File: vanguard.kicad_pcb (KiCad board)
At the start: 4 copper layers, 22 x 33.4 mm, 26 parts, among them J1 Conn_01x02, J2 USB_C_Receptacle, SW1 Switch_Tactile_CnK, U1 ATtiny3227-M, U2 MCP73831-2-OT, U5 AP63203WU

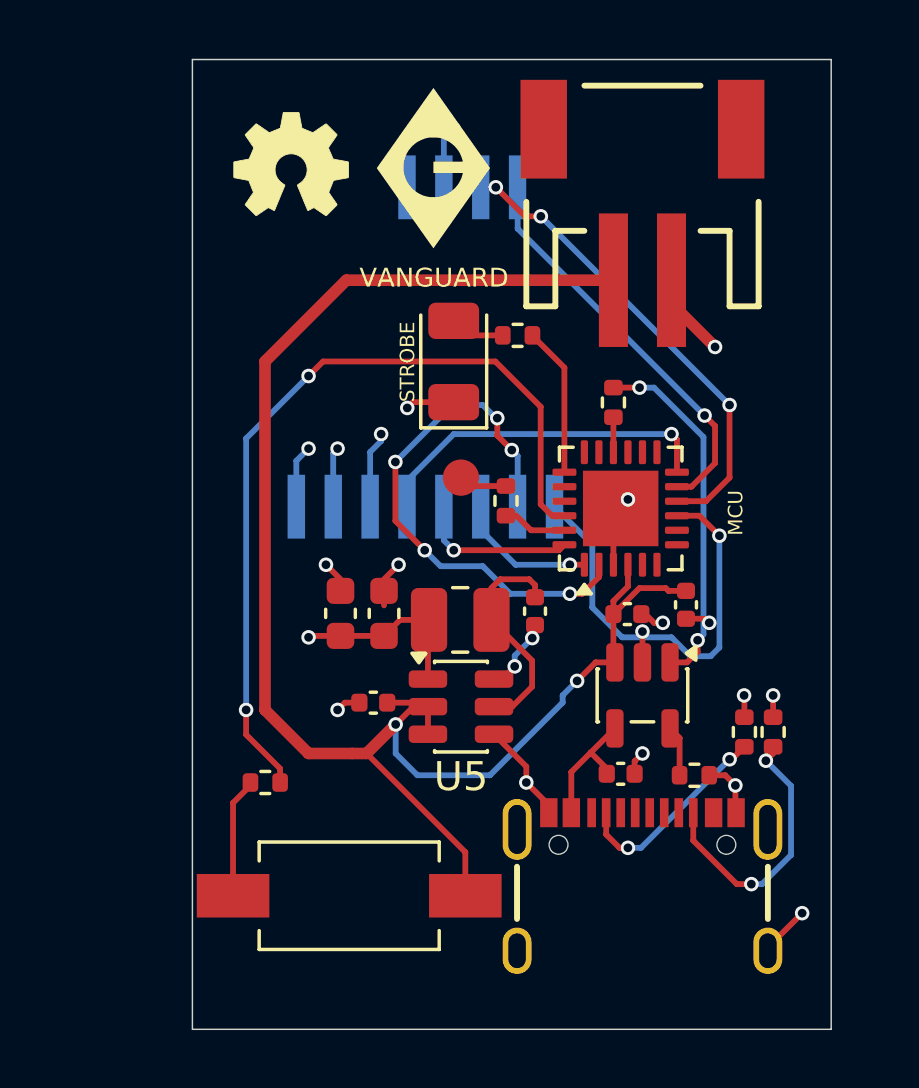
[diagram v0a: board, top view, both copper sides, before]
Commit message: basic code plus added UART
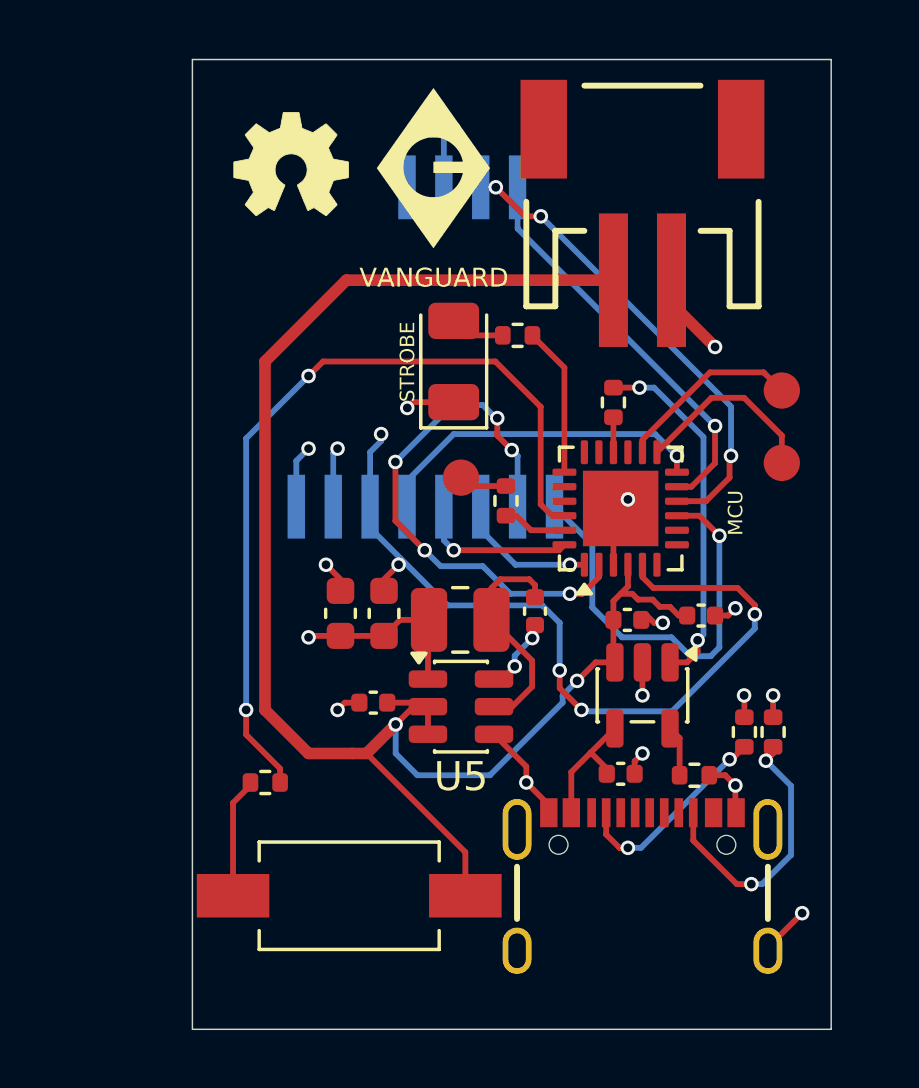
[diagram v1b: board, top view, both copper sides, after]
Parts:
- added TP2: 1.25mm, PCM_SparkFun-Connector:TestPoint-1.25mm, F.Cu at (147.3, 58.0)
- added TP3: 1.25mm, PCM_SparkFun-Connector:TestPoint-1.25mm, F.Cu at (147.3, 60.5)
- moved C2 0.64 mm to (144.5, 65.8), turned to 180 degrees
- moved C1 0.20 mm to (142.0, 65.9)
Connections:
- A1 pad 6: GND -> /SS
- U1 pad 13: unconnected-(U1-PB3-Pad13) -> /RX
- U1 pad 14: unconnected-(U1-PB2-Pad14) -> /TX
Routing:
- net /SS: track 0.00 -> 24.2 mm, vias 0 -> 3
- net /RX: track 0.00 -> 6.56 mm
- net /TX: track 0.00 -> 6.45 mm
- net GND: track 108.9 -> 113.1 mm
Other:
- board text added: "TX RX"

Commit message: done + optimizations
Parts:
- removed TP2, TP3: 1.25mm, PCM_SparkFun-Connector:TestPoint-1.25mm
- added J3: Conn_01x04_Pin, PCM_SparkFun-Connector:JST_1x04_P1.0mm_Horizontal_SMD, F.Cu at (127.1, 57.3)
- added J4: Conn_01x02, Connector_PinHeader_1.27mm:PinHeader_1x02_P1.27mm_Vertical, F.Cu at (148.2, 57.8)
- added REF**: MountingHole_2.2mm_M2_DIN965_Pad, MountingHole:MountingHole_2.2mm_M2_DIN965_Pad, F.Cu at (125.2, 49.2)
- added REF**: MountingHole_2.2mm_M2_DIN965_Pad, MountingHole:MountingHole_2.2mm_M2_DIN965_Pad, F.Cu at (125.2, 77.2)
- moved SW1 0.90 mm to (132.4, 74.5)
- moved J1 0.75 mm to (142.5, 49.8)
- moved R1 0.50 mm to (142.0, 58.4)
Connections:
- R1 pad 2: Net-(U1-PB0) -> Net-(U1-PB1)
- R6 pad 2: Net-(U1-PC2) -> Net-(U1-PC1)
- U1 pad 15: unconnected-(U1-PB1-Pad15) -> Net-(U1-PB1)
- U1 pad 16: Net-(U1-PB0) -> /SDA
- U1 pad 18: unconnected-(U1-PC1-Pad18) -> Net-(U1-PC1)
- U1 pad 19: Net-(U1-PC2) -> /SCL
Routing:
- net /SDA: track 0.00 -> 17.2 mm, vias 0 -> 2
- net /SCL: track 0.00 -> 16.5 mm, vias 0 -> 2
- net Net-(U1-PC2): track 5.17 -> 0.00 mm
- net 3.3V: track 15.1 -> 20.0 mm, vias 2 -> 3
- net Net-(U1-PC1): track 0.00 -> 4.78 mm
- net GND: track 113.1 -> 117.3 mm
- net Net-(U1-PB1): track 0.00 -> 1.20 mm
- net Net-(U1-PB0): track 1.20 -> 0.00 mm
- net Net-(R7-Pad2): track 4.15 -> 3.25 mm
- net /TX: track 6.45 -> 7.29 mm
- net VBATT: track 58.0 -> 57.5 mm
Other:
- board size 22 x 33.4 mm -> 27.5 x 33.4 mm
- board text added: "I2C"
- board text added: "UPDI"

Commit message: clean routing
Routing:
- net /RW_SW: track 14.8 -> 17.5 mm
- net /RX: track 6.35 -> 6.95 mm
- net /BUSY: track 16.4 -> 16.9 mm
- net VBATT: track 57.5 -> 58.0 mm

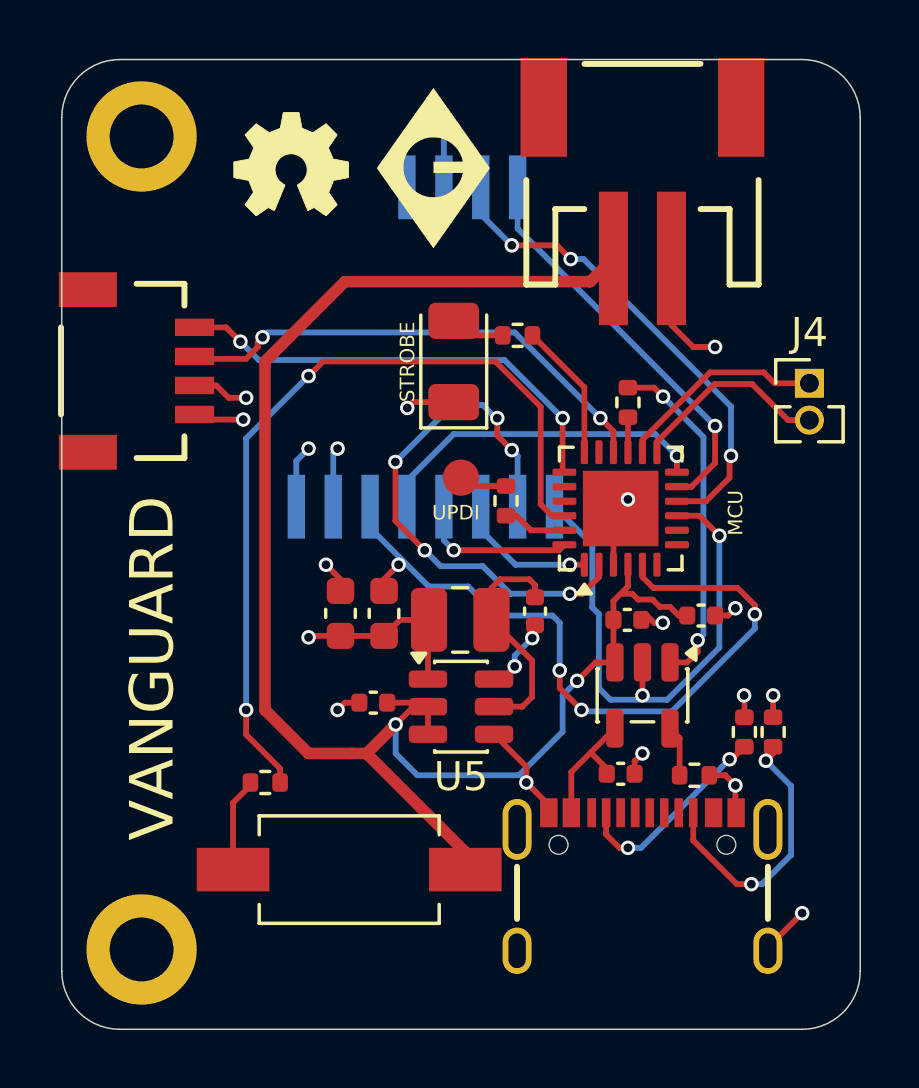
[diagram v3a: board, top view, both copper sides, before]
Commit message: cleaned up routing, fixed mistakes, implemented ETD initialization
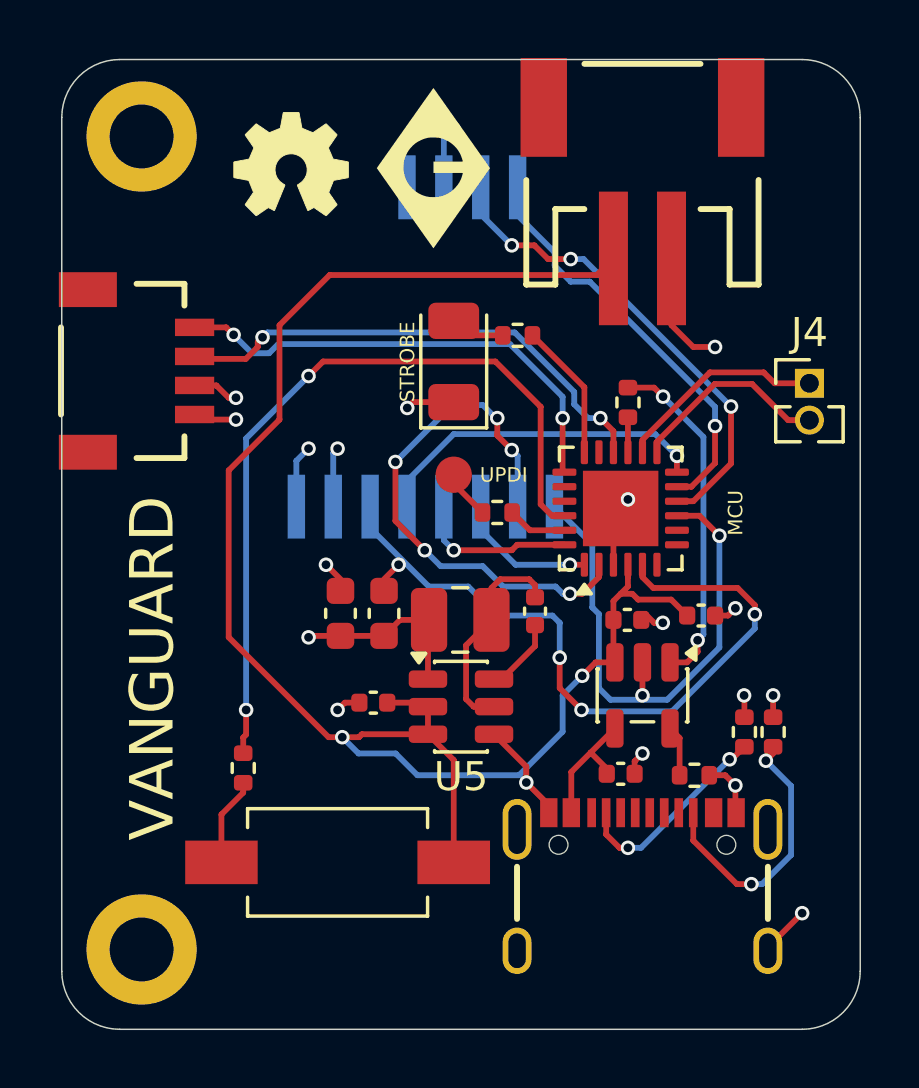
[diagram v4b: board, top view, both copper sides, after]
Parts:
- moved R7 0.91 mm to (128.8, 71.0), turned to -90 degrees
- moved R2 0.50 mm to (137.5, 62.2), turned to 180 degrees
- moved SW1 0.47 mm to (132.0, 74.2)
- moved TP1 0.27 mm to (136.0, 60.9)
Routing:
- net Net-(U1-PC5): track 28.6 -> 27.1 mm
- net VBATT: track 58.0 -> 59.4 mm
- net /SCL: track 16.5 -> 17.3 mm
- net Net-(U5-SW): track 7.91 -> 7.39 mm
- net Net-(U5-BST): track 2.60 -> 2.74 mm, vias 2 -> 0

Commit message: hw check 3
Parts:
- moved R3 2.33 mm to (144.9, 69.0), turned to -90 degrees
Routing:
- net GND: track 117.3 -> 119.9 mm, vias 18 -> 17
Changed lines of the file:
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@@
 	(footprint "PCM_SparkFun-Resistor:R_0402_1005Metric"
 		(layer "F.Cu")
-		(at 144.29 71.25 180)
+		(at 144.9 69 -90)
 		(descr "Resistor SMD 0402 (1005 Metric), square (rectangular) end terminal, IPC_7351 nominal, (Body size source: IPC-SM-782 page 72, https://www.pcb-3d.com/wordpress/wp-content/uploads/ipc-sm-782a_amendment_1_and_2.pdf), generated with kicad-footprint-generator")
 		(tags "SparkFun resistor")
 		(property "Reference" "R3"
-			(at 0 -1.17 0)
+			(at 0 -1.17 90)
 			(layer "F.Fab")
 			(effects
@@
 		)
 		(property "Value" "2.2k"
-			(at 0 1.17 0)
+			(at 0 1.17 90)
 			(layer "F.Fab")
 			(effects
@@
 		)
 		(property "Datasheet" "https://www.vishay.com/docs/20035/dcrcwe3.pdf"
-			(at 0 0 180)
+			(at 0 0 270)
 			(unlocked yes)
 			(layer "F.Fab")
@@
 		)
 		(property "Description" "Resistor"
-			(at 0 0 180)
+			(at 0 0 270)
 			(unlocked yes)
 			(layer "F.Fab")
@@
 		)
 		(property "PROD_ID" "RES-25566"
-			(at 0 0 180)
+			(at 0 0 270)
 			(unlocked yes)
 			(layer "F.Fab")
@@
 		)
 		(fp_line
-			(start 0.93 0.47)
-			(end -0.93 0.47)
+			(start -0.93 0.47)
+			(end -0.93 -0.47)
 			(stroke
 				(width 0.05)
@@
 		)
 		(fp_line
-			(start 0.93 -0.47)
-			(end 0.93 0.47)
+			(start 0.93 0.47)
+			(end -0.93 0.47)
 			(stroke
 				(width 0.05)
@@
 		)
 		(fp_line
-			(start -0.93 0.47)
-			(end -0.93 -0.47)
+			(start -0.93 -0.47)
+			(end 0.93 -0.47)
 			(stroke
 				(width 0.05)
@@
 		)
 		(fp_line
-			(start -0.93 -0.47)
-			(end 0.93 -0.47)
+			(start 0.93 -0.47)
+			(end 0.93 0.47)
 			(stroke
 				(width 0.05)
@@
 		)
 		(fp_line
-			(start 0.525 0.27)
-			(end -0.525 0.27)
+			(start -0.525 0.27)
+			(end -0.525 -0.27)
 			(stroke
 				(width 0.1)
@@
 		)
 		(fp_line
-			(start 0.525 -0.27)
-			(end 0.525 0.27)
+			(start 0.525 0.27)
+			(end -0.525 0.27)
 			(stroke
 				(width 0.1)
@@
 		)
 		(fp_line
-			(start -0.525 0.27)
-			(end -0.525 -0.27)
+			(start -0.525 -0.27)
+			(end 0.525 -0.27)
 			(stroke
 				(width 0.1)
@@
 		)
 		(fp_line
-			(start -0.525 -0.27)
-			(end 0.525 -0.27)
+			(start 0.525 -0.27)
+			(end 0.525 0.27)
 			(stroke
 				(width 0.1)
@@
 		)
 		(pad "1" smd roundrect
-			(at -0.51 0 180)
+			(at -0.51 0 270)
 			(size 0.54 0.64)
 			(layers "F.Cu" "F.Mask" "F.Paste")
@@
 		)
 		(pad "2" smd roundrect
-			(at 0.51 0 180)
+			(at 0.51 0 270)
 			(size 0.54 0.64)
 			(layers "F.Cu" "F.Mask" "F.Paste")
@@
 	)
 	(gr_text "MCU"
-		(at 146 63 90)
+		(at 146.2 63 90)
 		(layer "F.SilkS")
 		(effects
@@
 	)
 	(segment
-		(start 141.5 64)
-		(end 141.5 62.3125)
+		(start 142.89 68.49)
+		(end 144.9 68.49)
 		(width 0.2)
 		(layer "F.Cu")
@@
 	)
 	(segment
-		(start 145.35 71.25)
-		(end 144.8 71.25)
+		(start 141.5 64)
+		(end 141.5 62.3125)
 		(width 0.2)
 		(layer "F.Cu")
@@
 	)
 	(segment
+		(start 141.747059 68.475)
+		(end 142.5 67.722059)
+		(width 0.2)
+		(layer "F.Cu")
+		(net "GND")
+	)
+	(segment
 		(start 145.45 65.75)
 		(end 145.7 65.5)
@@
 	)
 	(segment
-		(start 143.2 66)
-		(end 142.9 66)
+		(start 142.5 67.3625)
+		(end 142.5 68.1)
 		(width 0.2)
 		(layer "F.Cu")
@@
 	)
 	(segment
-		(start 139.275 72.54)
-		(end 139.275 72.275)
+		(start 143.2 66)
+		(end 142.9 66)
 		(width 0.2)
 		(layer "F.Cu")
@@
 	)
 	(segment
-		(start 145.7 71.6)
-		(end 145.35 71.25)
+		(start 139.275 72.54)
+		(end 139.275 72.275)
 		(width 0.2)
 		(layer "F.Cu")
@@
 	)
 	(segment
-		(start 145.7 71.6)
-		(end 145.7 72.25)
-		(width 0.2)
-		(layer "F.Cu")
-		(net "GND")
-	)
-	(segment
 		(start 145 65.75)
 		(end 145.45 65.75)
@@
 	)
 	(segment
-		(start 142.5 67.3625)
-		(end 142.5 68.5)
-		(width 0.2)
-		(layer "F.Cu")
-		(net "GND")
-	)
-	(segment
 		(start 138.5 70.95)
 		(end 138.5 71.5)
@@
 	)
 	(segment
+		(start 142.5 68.1)
+		(end 142.89 68.49)
+		(width 0.2)
+		(layer "F.Cu")
+		(net "GND")
+	)
+	(segment
 		(start 144.25 56.5)
 		(end 145 56.5)
@@
 	)
 	(segment
+		(start 141.433266 68.475)
+		(end 141.747059 68.475)
+		(width 0.2)
+		(layer "F.Cu")
+		(net "GND")
+	)
+	(segment
 		(start 146.818 77.295)
 		(end 146.818 77.182)
@@
 	)
 	(segment
+		(start 142.5 67.722059)
+		(end 142.5 67.3625)
+		(width 0.2)
+		(layer "F.Cu")
+		(net "GND")
+	)
+	(segment
 		(start 146.01 69.25)
 		(end 146.01 68.51)
@@
 	)
 	(via blind
-		(at 142.5 68.5)
-		(size 0.5)
-		(drill 0.3)
-		(layers "F.Cu" "In1.Cu")
-		(net "GND")
-	)
-	(via blind
 		(at 147 68.5)
 		(size 0.5)
@@
 	)
 	(via blind
-		(at 138.5 71.5)
+		(at 141.433266 68.475)
 		(size 0.5)
 		(drill 0.3)
@@
 	)
 	(via blind
-		(at 145.7 71.6)
+		(at 138.5 71.5)
 		(size 0.5)
 		(drill 0.3)
@@
 	)
 	(segment
+		(start 141.433266 68.475)
+		(end 142.9 67.008266)
+		(width 0.2)
+		(layer "In1.Cu")
+		(net "GND")
+	)
+	(segment
 		(start 142.5 70.5)
 		(end 143.25 71.25)
@@
 	)
 	(segment
-		(start 142.9 68.1)
+		(start 142.9 67.008266)
 		(end 142.9 66.3)
 		(width 0.2)
@@
 	)
 	(segment
-		(start 142.5 68.5)
-		(end 142.9 68.1)
-		(width 0.2)
-		(layer "In1.Cu")
-		(net "GND")
-	)
-	(segment
 		(start 131.6 64)
 		(end 133 64)
@@
 	)
 	(segment
-		(start 140.425 67.825)
-		(end 140.8875 67.3625)
+		(start 143.49 65.2)
+		(end 142.707428 65.2)
 		(width 0.2)
 		(layer "F.Cu")
@@
 	)
 	(segment
-		(start 144.04 65.75)
-		(end 143.49 65.2)
+		(start 140.425 67.825)
+		(end 140.8875 67.3625)
 		(width 0.2)
 		(layer "F.Cu")
@@
 	)
 	(segment
+		(start 144.04 65.75)
+		(end 143.49 65.2)
+		(width 0.2)
+		(layer "F.Cu")
+		(net "VBATT")
+	)
+	(segment
 		(start 140.927818 54.022182)
 		(end 141.5 53.45)
@@
 	)
 	(segment
+		(start 142.507429 65)
+		(end 141.75 65)
+		(width 0.2)
+		(layer "F.Cu")
+		(net "VBATT")
+	)
+	(segment
 		(start 142 64.75)
 		(end 141.75 65)
@@
 	)
 	(segment
-		(start 143.49 65.2)
-		(end 142.35 65.2)
-		(width 0.2)
-		(layer "F.Cu")
-		(net "VBATT")
-	)
-	(segment
-		(start 142.35 65.2)
-		(end 142.15 65)
-		(width 0.2)
-		(layer "F.Cu")
-		(net "VBATT")
-	)
-	(segment
-		(start 142.15 65)
-		(end 141.75 65)
-		(width 0.2)
-		(layer "F.Cu")
-		(net "VBATT")
-	)
-	(segment
 		(start 132.161091 69.938909)
 		(end 131.688909 69.938909)
@@
 	)
 	(segment
+		(start 142.707428 65.2)
+		(end 142.507429 65)
+		(width 0.2)
+		(layer "F.Cu")
+		(net "VBATT")
+	)
+	(segment
 		(start 134.975 68.75)
 		(end 135.1125 68.8875)
@@
 	)
 	(segment
-		(start 143.78 69.9675)
-		(end 143.78 71.25)
+		(start 144.2625 69.6375)
+		(end 143.45 69.6375)
+		(width 0.2)
+		(layer "F.Cu")
+		(net "Net-(U2-PROG)")
+	)
+	(segment
+		(start 144.9 69.51)
+		(end 144.39 69.51)
 		(width 0.2)
 		(layer "F.Cu")
@@
 	)
 	(segment
-		(start 143.45 69.6375)
-		(end 143.78 69.9675)
+		(start 144.39 69.51)
+		(end 144.2625 69.6375)
 		(width 0.2)
 		(layer "F.Cu")
